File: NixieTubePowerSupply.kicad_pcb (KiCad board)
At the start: 2 copper layers, 72 x 48 mm, 37 parts, among them J1 Barrel_Jack_Switch, J10 Conn_01x02_Pin, J11 Screw_Terminal_01x02, J2 Conn_01x02_Pin, J3 Screw_Terminal_01x02, J4 Conn_01x03_Pin, J5 Conn_01x03_Pin, J6 Screw_Terminal_01x03, J7 Conn_01x02_Pin, J8 Conn_01x02_Pin, J9 Conn_01x02_Pin, Q1 2SA1015, Q2 TK10A60D, U1 NJM7805, U2 NJM2360AD

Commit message: 配置を完了
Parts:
- removed J11: Screw_Terminal_01x02, mylib:TerminalBlock_TB111-2-2_P5.08mm
- D1: value 1N4148 -> 4148
- moved J4 11.5 mm to (59.1, 29.5)
- moved J5 10.4 mm to (69.1, 30.7), turned to -90 degrees
- moved C7 10.2 mm to (9.94, 33.7)
- moved C1 6.33 mm to (2.99, 33.7)
- moved U1 4.43 mm to (17.7, 39.7)
- moved J7 3.64 mm to (58.8, 37.3), turned to 180 degrees
- moved J10 3.38 mm to (58.8, 45.1), turned to 180 degrees
- moved RV1 3.08 mm to (20.9, 35.2)
- moved R5 3.05 mm to (36.4, 34.8)
- moved J8 2.98 mm to (47.1, 37.3), turned to 180 degrees
- moved R6 2.89 mm to (26.2, 30.6)
- moved J9 2.58 mm to (47.1, 45.1), turned to 180 degrees
- moved C6 2.34 mm to (14.6, 46.0)
- moved C8 2.32 mm to (54.0, 5.70), turned to 0 degrees
- moved C2 2.27 mm to (2.99, 12.7), turned to 0 degrees
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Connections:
- J6 pad 1: /200V -> GND
- J6 pad 3: GND -> /200V
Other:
- board text added: "1015"
- board text added: "2SA"

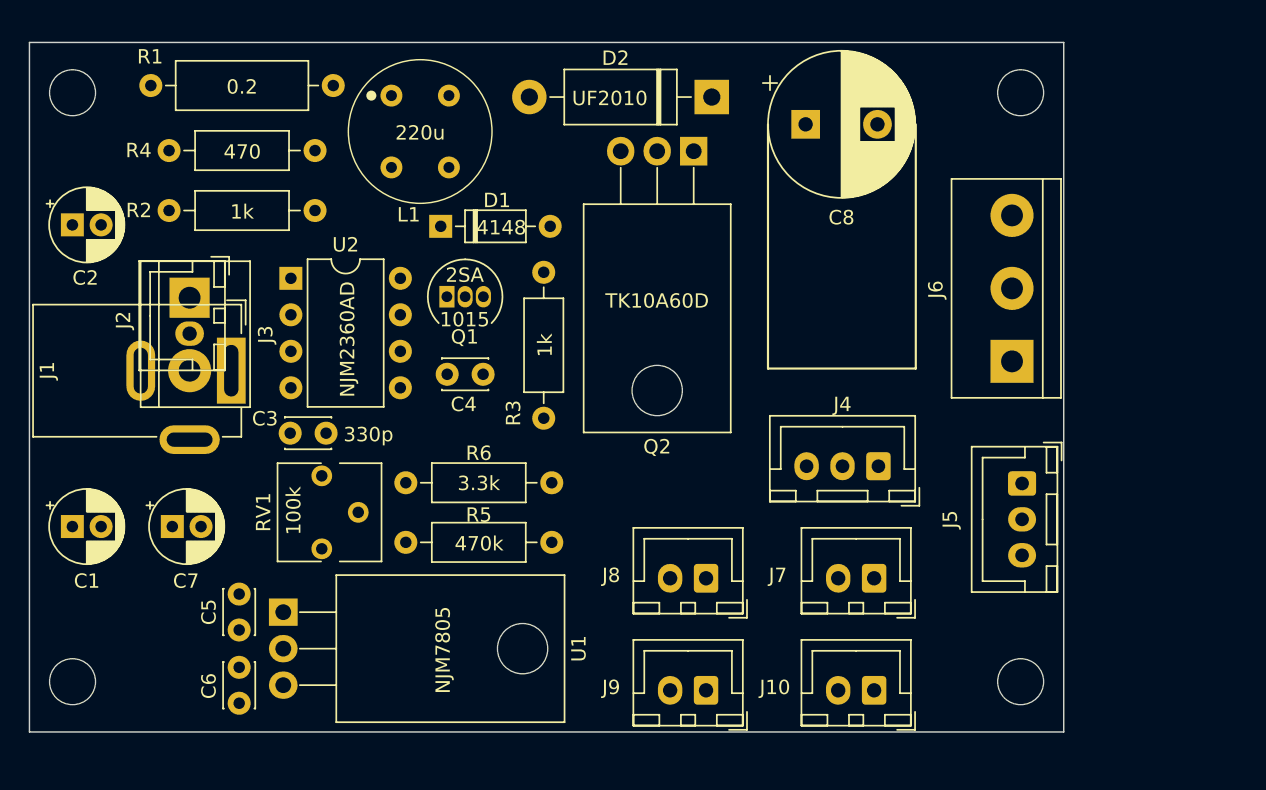
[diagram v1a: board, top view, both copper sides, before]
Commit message: 配線を完了
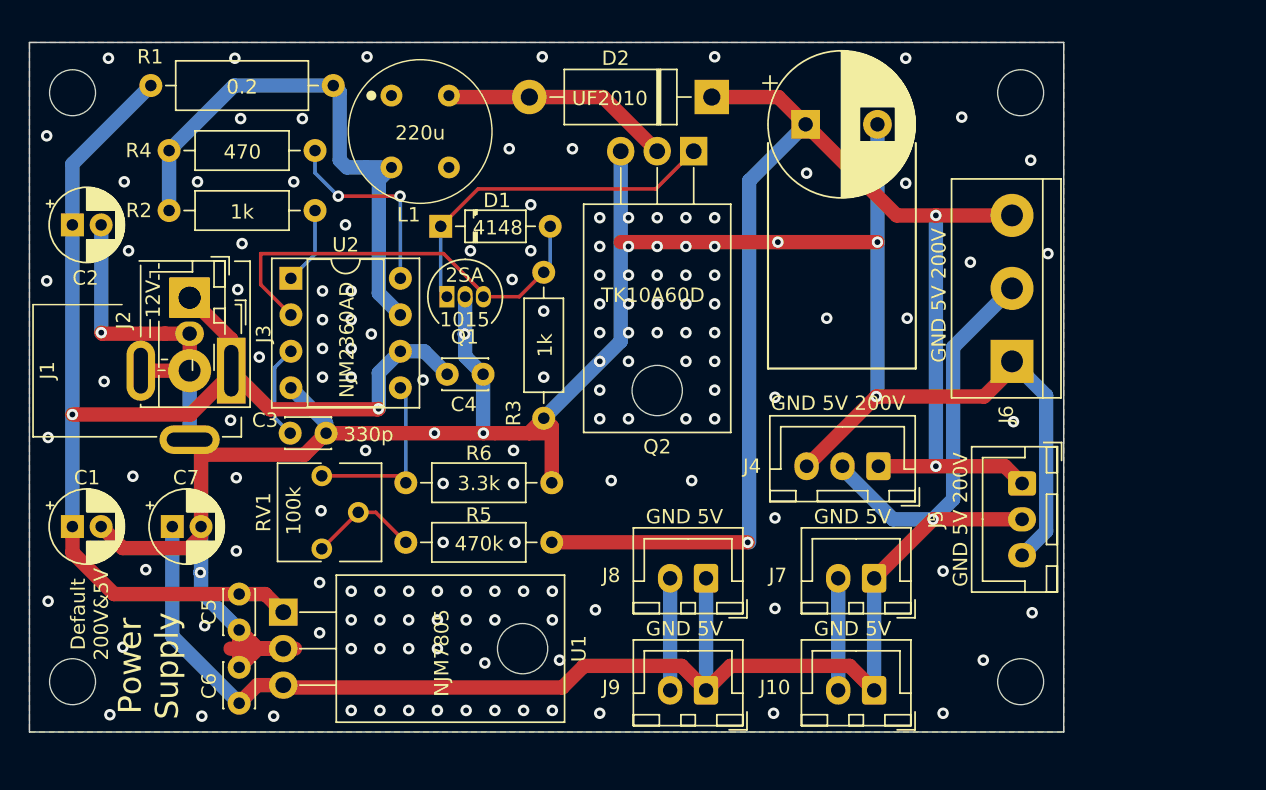
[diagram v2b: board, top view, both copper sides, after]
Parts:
- U2: footprint Package_DIP:DIP-8_W7.62mm -> Package_DIP:DIP-8_W7.62mm_Socket
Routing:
- net GND: track 0.00 -> 213.1 mm, vias 0 -> 153
- net /5V: track 0.00 -> 115.6 mm, vias 0 -> 1
- net /200V: track 0.00 -> 96.6 mm, vias 0 -> 3
- net /12V: track 0.00 -> 89.6 mm, vias 0 -> 2
- net Net-(U2-SI): track 0.00 -> 39.2 mm
- net Net-(D1-A): track 0.00 -> 30.3 mm
- net Net-(D1-K): track 0.00 -> 24.9 mm
- net Net-(D2-A): track 0.00 -> 16.1 mm
- net Net-(U2-CD): track 0.00 -> 13.9 mm, vias 0 -> 2
- net Net-(U2-INV): track 0.00 -> 12.8 mm
- net Net-(R5-Pad2): track 0.00 -> 7.77 mm
- net Net-(U2-CT): track 0.00 -> 6.61 mm
- net Net-(U2-CS): track 0.00 -> 5.42 mm
- added copper zone on B.Cu, net GND
- added copper zone on F.Cu, net GND
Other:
- board text added: "12V"
- board text added: "Default 200V&5V"
- board text added: "GND 5V"
- board text added: "GND 5V 200V"
- board text added: "Power Supply"

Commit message: 基板サイズを共有のものに変更
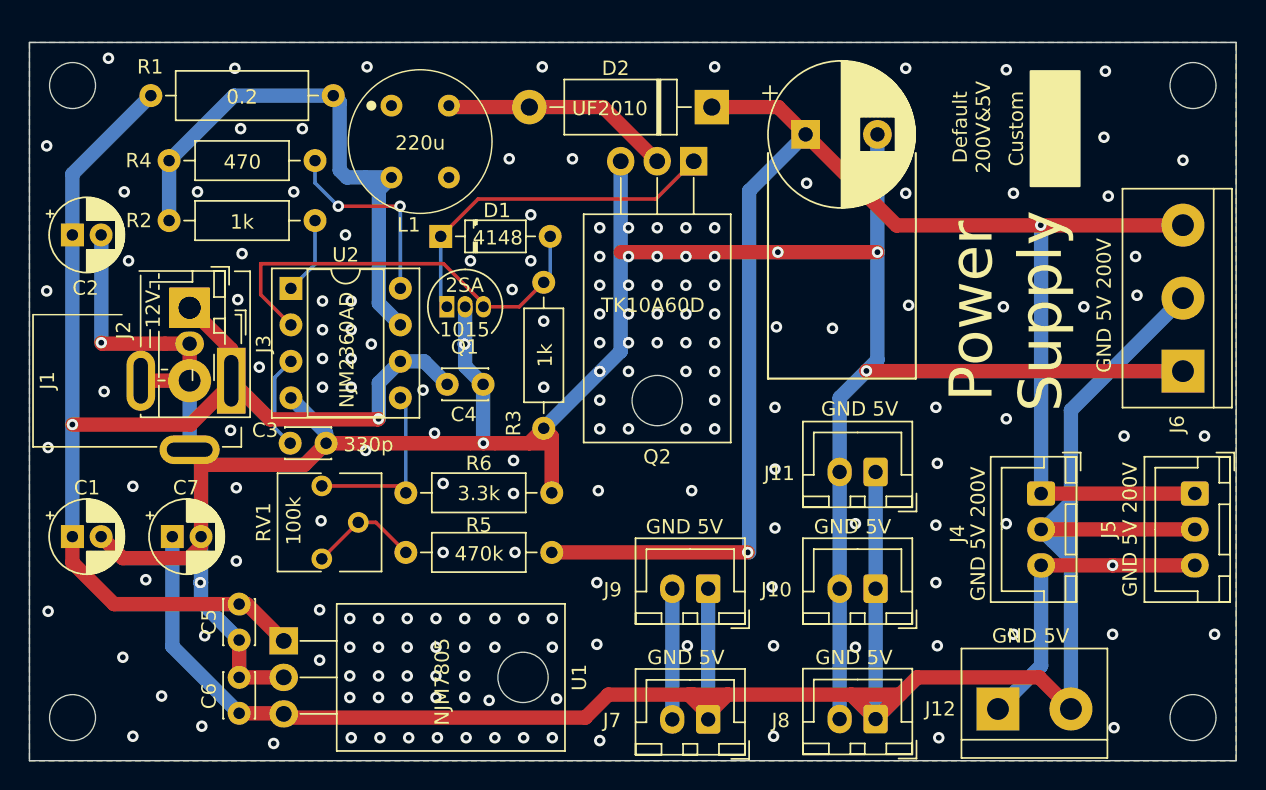
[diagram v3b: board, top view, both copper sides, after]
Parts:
- removed the ? at (69.0, 3.50)
- removed the ? at (3.00, 44.5)
- removed the ? at (3.00, 3.50)
- removed the ? at (69.0, 44.5)
- added ?: , MountingHole:MountingHole_3.2mm_M3, F.Cu at (81.0, 47.0)
- added ?: , MountingHole:MountingHole_3.2mm_M3, F.Cu at (3.00, 3.00)
- added ?: , MountingHole:MountingHole_3.2mm_M3, F.Cu at (3.00, 47.0)
- added ?: , MountingHole:MountingHole_3.2mm_M3, F.Cu at (81.0, 3.00)
- added J11: Conn_01x02_Pin, Connector_JST:JST_XH_B2B-XH-A_1x02_P2.50mm_Vertical, F.Cu at (58.9, 29.9)
- added J12: Screw_Terminal_01x02, mylib:TerminalBlock_TB111-2-2_P5.08mm, F.Cu at (67.4, 46.0)
- moved J8 15.3 mm to (58.9, 47.1)
- moved J7 15.2 mm to (47.2, 47.1)
- moved J5 12.0 mm to (81.1, 31.4)
- moved J6 11.9 mm to (79.9, 22.9)
- moved J4 11.5 mm to (70.4, 31.4), turned to -90 degrees
- moved J9 7.08 mm to (47.2, 38.0)
- moved J10 7.08 mm to (58.9, 38.0)
- moved U1 2.00 mm to (17.7, 41.7)
- moved C5 0.70 mm to (14.6, 39.1)
- moved C6 0.70 mm to (14.6, 46.7)
- moved R5 0.70 mm to (36.4, 35.5)
- moved R6 0.70 mm to (26.2, 31.4)
- moved RV1 0.70 mm to (20.9, 36.0)
- moved C2 0.70 mm to (2.99, 13.4)
- moved R2 0.70 mm to (9.72, 12.4)
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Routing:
- net /5V: track 115.6 -> 166.2 mm, vias 1 -> 0
- net GND: track 213.1 -> 233.9 mm, vias 153 -> 182
- net /200V: track 96.6 -> 110.0 mm, vias 3 -> 2
- net /12V: track 89.6 -> 90.2 mm
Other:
- board size 72 x 48 mm -> 84 x 50 mm
- board text added: "Custom"

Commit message: 製造後データを追加
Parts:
- added D1: ON, LED_THT:LED_D3.0mm, F.Cu at (4.00, 7.10)
- added R1: 10k, Resistor_THT:R_Axial_DIN0207_L6.3mm_D2.5mm_P10.16mm_Horizontal, F.Cu at (8.50, 2.92)
- added SW1: SW_SPDT, mylib:Switch_Toggle_2MS1-T1-B4-M2-Q-E, F.Cu at (5.54, 40.9)
- moved RV1 5.25 mm to (19.8, 30.8), turned to 180 degrees
- moved L1 2.90 mm to (30.1, 6.90)
- moved R2 2.85 mm to (11.3, 3.70)
- moved R3 2.85 mm to (12.6, 12.4)
- moved R5 2.85 mm to (12.6, 8.22)
- moved D3 2.05 mm to (49.5, 4.50)
- moved C1 1.70 mm to (3.00, 32.7)
- moved C7 1.70 mm to (9.96, 32.7)
- moved C2 1.10 mm to (2.99, 14.5)
- moved D2 0.36 mm to (29.0, 13.5)
- renumbered D1 to D2, D2 to D3, R1 to R2, R2 to R3, R3 to R4, R4 to R5, R5 to R6, R6 to R7
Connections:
- C1 pad 1: /12V -> Net-(#FLG03-pwr)
- C2 pad 1: /12V -> Net-(#FLG03-pwr)
- C4 pad 1: /12V -> Net-(#FLG03-pwr)
- C5 pad 1: /12V -> Net-(#FLG03-pwr)
- R2 pad 1: /12V -> Net-(#FLG03-pwr)
- R6 pad 2: Net-(R5-Pad2) -> Net-(R6-Pad2)
- RV1 pad 1: Net-(R5-Pad2) -> Net-(U2-INV)
- RV1 pad 2: Net-(R5-Pad2) -> Net-(R6-Pad2)
- RV1 pad 3: Net-(U2-INV) -> Net-(R6-Pad2)
- U1 pad 1: /12V -> Net-(#FLG03-pwr)
- U2 pad 6: /12V -> Net-(#FLG03-pwr)
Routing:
- net Net-(#FLG03-pwr): track 0.00 -> 89.5 mm
- net /12V: track 90.2 -> 28.9 mm, vias 2 -> 0
- net Net-(R6-Pad2): track 0.00 -> 8.25 mm
- net Net-(R5-Pad2): track 7.77 -> 0.00 mm
- net Net-(D1-K): track 0.00 -> 6.23 mm
- net /5V: track 166.2 -> 170.1 mm
- net Net-(U2-CD): track 13.9 -> 10.2 mm, vias 2 -> 0
- net Net-(U2-SI): track 39.2 -> 36.1 mm
- net GND: track 233.9 -> 236.9 mm, vias 182 -> 177
- net Net-(D3-A): track 16.1 -> 13.2 mm
- net /200V: track 110.0 -> 107.9 mm
- net Net-(U2-CS): track 5.42 -> 6.60 mm
- net Net-(U2-INV): track 12.8 -> 13.9 mm
- net Net-(D2-K): track 24.9 -> 24.3 mm
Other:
- board text added: "Default 200V,10mA & 5V,1A"
- board text added: "JLCJLCJLCJLC"
- board text added: "SL：ON⇔OFF"
- board text added: "TG：OFF⇔ON"
- board text added: "by T.N."
- board text removed: "Default 200V&5V"
